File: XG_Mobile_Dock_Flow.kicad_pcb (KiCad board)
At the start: 4 copper layers, 220 x 65 mm, 111 parts, among them J1 5-1775443-8, J10 SWD, J11 UART, J12 I2C1, J13 39300240, J14 469911008, J17 8730, J2 20455-040E-76, J3 20455-040E-76, J4 3-2362375-4, J5 USB_C_Receptacle, Q16 AO3401A, Q17 2N7002W, SW1 SW_Push, U1 DS160PR410RNQR, U12 STM32F030C8Tx, U2 DS160PR410RNQR

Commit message: slight correction to 3.3v trace
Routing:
- net +3V3: track 237.6 -> 231.3 mm
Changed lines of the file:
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@@
-	)
-	(segment
-		(start 143.6 92.725)
-		(end 147.825 88.5)
-		(width 2.045295)
-		(layer "In1.Cu")
-		(net 2)
 	)
 	(segment
@@
 	)
 	(segment
-		(start 91.079446 78.920554)
-		(end 84.917496 72.758603)
-		(width 1.5)
+		(start 86.075 63.377496)
+		(end 85.382504 63.377496)
+		(width 2.045295)
 		(layer "In1.Cu")
 		(net 2)
@@
 	)
 	(segment
-		(start 147.825 83.040678)
-		(end 154.33666 76.529018)
-		(width 2.045295)
-		(layer "In1.Cu")
-		(net 2)
-	)
-	(segment
-		(start 104.883893 92.725)
-		(end 143.6 92.725)
-		(width 2.045295)
+		(start 84.917496 72.758604)
+		(end 84.917496 71.057504)
+		(width 1.5)
 		(layer "In1.Cu")
 		(net 2)
@@
 		(end 101.025 80.875)
 		(width 1.5)
+		(layer "In1.Cu")
+		(net 2)
+	)
+	(segment
+		(start 143.6 92.725)
+		(end 147.825 88.5)
+		(width 2.045295)
 		(layer "In1.Cu")
 		(net 2)
@@
 	)
 	(segment
-		(start 154.33666 76.529018)
-		(end 169.83666 76.529018)
-		(width 2.045295)
-		(layer "In1.Cu")
-		(net 2)
-	)
-	(segment
 		(start 98.425 74.025)
 		(end 95.975 74.025)
@@
 	)
 	(segment
+		(start 85.15 72.991107)
+		(end 104.883893 92.725)
+		(width 2.045295)
+		(layer "In1.Cu")
+		(net 2)
+	)
+	(segment
+		(start 105.275 79.425)
+		(end 105.275 80.875)
+		(width 1.5)
+		(layer "In1.Cu")
+		(net 2)
+	)
+	(segment
+		(start 107.925 80.875)
+		(end 105.275 80.875)
+		(width 0.8)
+		(layer "In1.Cu")
+		(net 2)
+	)
+	(segment
 		(start 147.825 88.5)
 		(end 147.825 83.040678)
@@
 	)
 	(segment
-		(start 84.917496 72.758603)
-		(end 104.312893 92.154)
-		(width 2.045295)
-		(layer "In1.Cu")
-		(net 2)
-	)
-	(segment
-		(start 105.275 79.425)
-		(end 105.275 80.875)
-		(width 1.5)
-		(layer "In1.Cu")
-		(net 2)
-	)
-	(segment
-		(start 107.925 80.875)
-		(end 105.275 80.875)
-		(width 0.8)
+		(start 147.825 83.040678)
+		(end 154.33666 76.529018)
+		(width 2.045295)
 		(layer "In1.Cu")
 		(net 2)
@@
 		(end 97.029446 84.870554)
 		(width 1.5)
+		(layer "In1.Cu")
+		(net 2)
+	)
+	(segment
+		(start 154.33666 76.529018)
+		(end 169.83666 76.529018)
+		(width 2.045295)
+		(layer "In1.Cu")
+		(net 2)
+	)
+	(segment
+		(start 104.883893 92.725)
+		(end 143.6 92.725)
+		(width 2.045295)
 		(layer "In1.Cu")
 		(net 2)
@@
 	)
 	(segment
-		(start 84.917496 63.377496)
-		(end 84.917496 72.758603)
-		(width 2.045295)
-		(layer "In1.Cu")
-		(net 2)
-	)
-	(segment
-		(start 104.312893 92.154)
-		(end 104.883893 92.725)
+		(start 85.15 63.61)
+		(end 85.15 72.526099)
+		(width 2.045295)
+		(layer "In1.Cu")
+		(net 2)
+	)
+	(segment
+		(start 85.15 70.825)
+		(end 85.15 72.991107)
+		(width 2.045295)
+		(layer "In1.Cu")
+		(net 2)
+	)
+	(segment
+		(start 85.382504 63.377496)
+		(end 85.15 63.61)
 		(width 2.045295)
 		(layer "In1.Cu")
@@
 	)
 	(segment
-		(start 84.917496 63.377496)
-		(end 86.917496 63.377496)
-		(width 1.5)
-		(layer "In1.Cu")
+		(start 84.917496 71.057504)
+		(end 85.15 70.825)
+		(width 1.5)
+		(layer "In1.Cu")

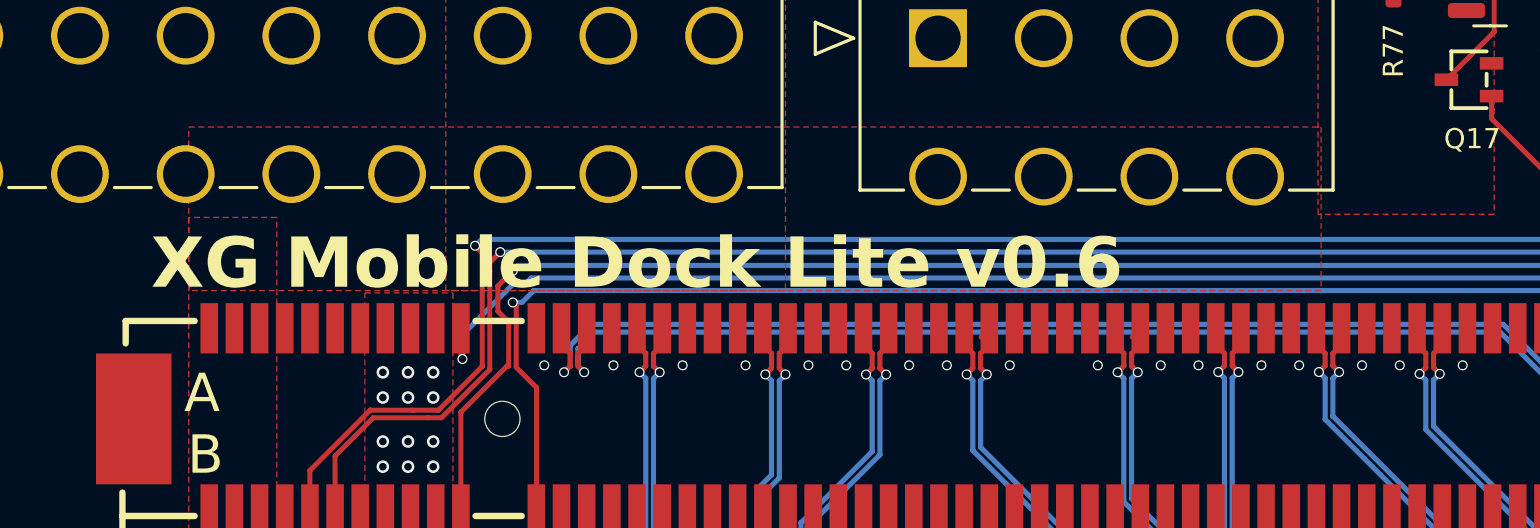
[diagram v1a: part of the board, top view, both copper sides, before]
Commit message: added proper text on board
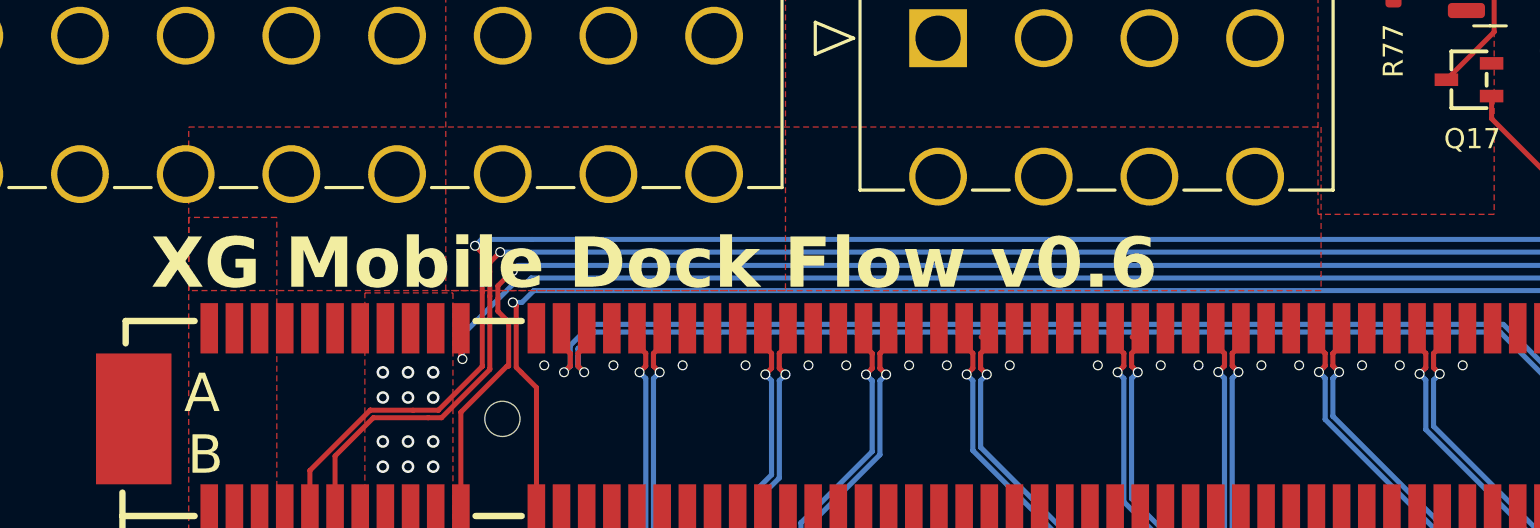
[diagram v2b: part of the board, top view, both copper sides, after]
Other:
- board text added: "XG Mobile Dock Flow v0.6"
- board text removed: "XG Mobile Dock Lite v0.6"
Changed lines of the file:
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@@
 		)
 	)
-	(gr_text "XG Mobile Dock Lite v0.6"
+	(gr_text "XG Mobile Dock Flow v0.6"
 		(at 75.621496 55.121496 0)
 		(layer "F.SilkS")

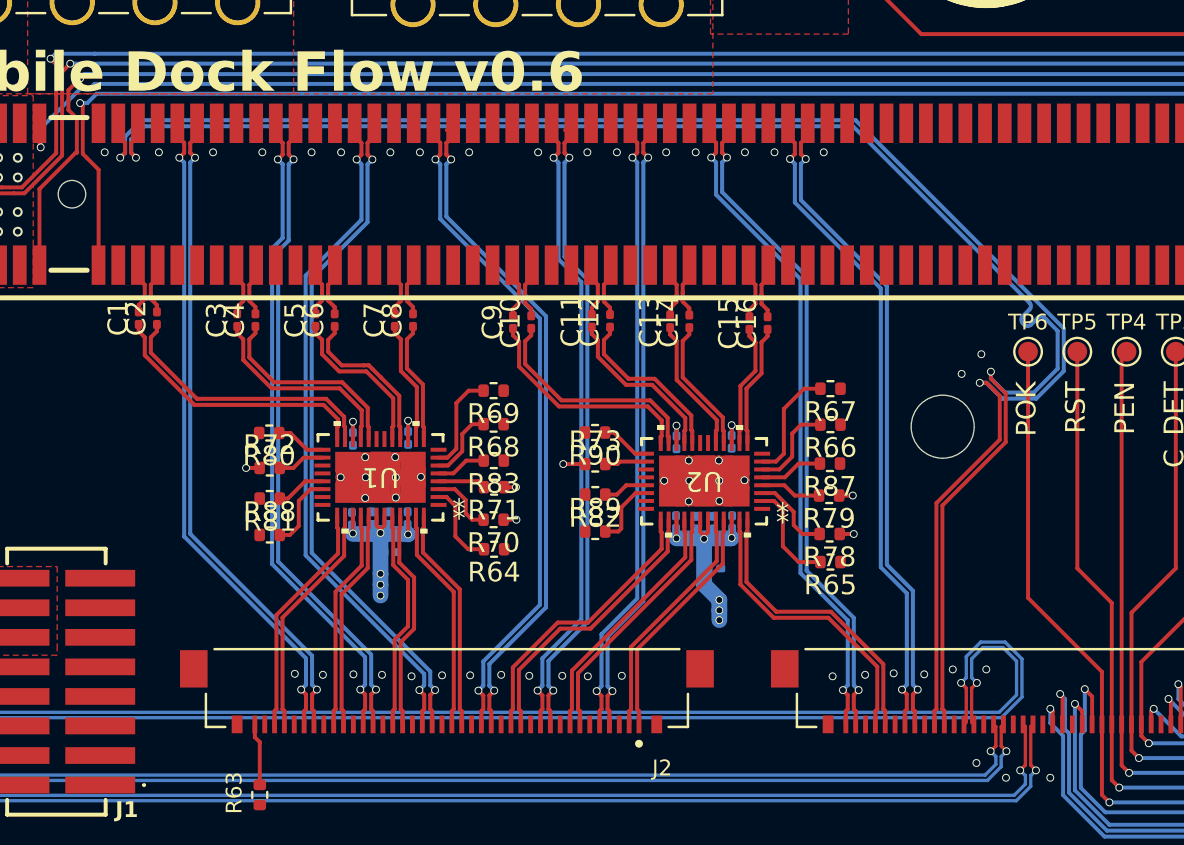
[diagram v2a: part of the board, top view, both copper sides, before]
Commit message: better routing of the pcie clock trace
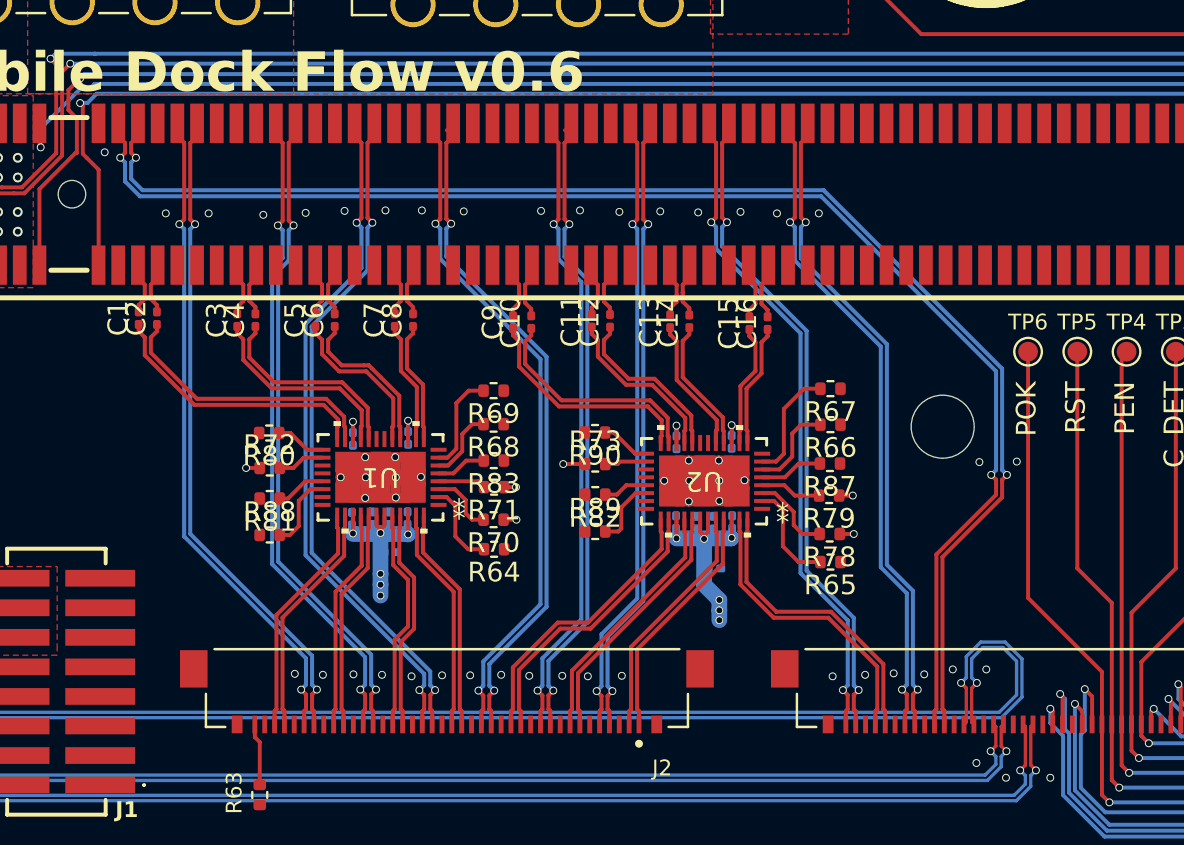
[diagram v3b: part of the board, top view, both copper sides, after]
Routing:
- net /CLKP: track 82.4 -> 71.0 mm
- net /CLKN: track 82.3 -> 71.0 mm

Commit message: final changes, still need to recheck
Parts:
- removed J16: ~, Connector_JST:JST_PH_S2B-PH-K_1x02_P2.00mm_Horizontal
- removed R74: 47k, Resistor_SMD:R_0402_1005Metric
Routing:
- net GND: vias 66 -> 76

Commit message: more preparations for building the board
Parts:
- C1, C10, C11, C12, C13, C14, C15, C16, C2, C3, C4, C5, C6, C7, C8, C9: value 0.22μF -> 220nF
- C17, C18, C19, C20, C22, C23, C24, C25: value 0.1μF -> 100nF
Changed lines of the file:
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@@
 			(outputformat 1)
 			(mirror no)
-			(drillshape 1)
+			(drillshape 0)
 			(scaleselection 1)
-			(outputdirectory "")
+			(outputdirectory "../XG_Mobile_Station_Release/")
 		)
 	)
@@
 			)
 		)
-		(property "Value" "0.22μF"
+		(property "Value" "220nF"
 			(at 0 1.05 90)
 			(layer "F.Fab")
@@
 			)
 		)
-		(property "Value" "0.22μF"
+		(property "Value" "220nF"
 			(at 0 1.05 90)
 			(layer "F.Fab")
@@
 		(sheetname "/")
 		(sheetfile "XG_Mobile_Dock_Flow.kicad_sch")
-		(attr through_hole exclude_from_pos_files)
+		(attr through_hole)
 		(fp_line
 			(start 4.877981 0.635)
@@
 			)
 		)
-		(property "Value" "0.22μF"
+		(property "Value" "220nF"
 			(at 0 1.05 90)
 			(layer "F.Fab")
@@
 			)
 		)
-		(property "Value" "0.22μF"
+		(property "Value" "220nF"
 			(at 0 1.05 90)
 			(layer "F.Fab")
@@
 			)
 		)
-		(property "Value" "0.22μF"
+		(property "Value" "220nF"
 			(at 0 1.05 90)
 			(layer "F.Fab")
@@
 			)
 		)
-		(property "Value" "0.22μF"
+		(property "Value" "220nF"
 			(at 0 1.05 90)
 			(layer "F.Fab")
@@
 			)
 		)
-		(property "Value" "0.22μF"
+		(property "Value" "220nF"
 			(at 0 1.05 90)
 			(layer "F.Fab")
@@
 			)
 		)
-		(property "Value" "0.22μF"
+		(property "Value" "220nF"
 			(at 0 1.05 90)
 			(layer "F.Fab")
@@
 			)
 		)
-		(property "Value" "0.22μF"
+		(property "Value" "220nF"
 			(at 0 1.05 90)
 			(layer "F.Fab")
@@
 			)
 		)
-		(property "Value" "0.22μF"
+		(property "Value" "220nF"
 			(at 0 1.05 90)
 			(layer "F.Fab")
@@
 			)
 		)
-		(property "Value" "0.22μF"
+		(property "Value" "220nF"
 			(at 0 1.05 90)
 			(layer "F.Fab")
@@
 			)
 		)
-		(property "Value" "0.22μF"
+		(property "Value" "220nF"
 			(at 0 1.05 90)
 			(layer "F.Fab")
@@
 			)
 		)
-		(property "Value" "0.22μF"
+		(property "Value" "220nF"
 			(at 0 1.05 90)
 			(layer "F.Fab")
@@
 			)
 		)
-		(property "Value" "0.22μF"
+		(property "Value" "220nF"
 			(at 0 1.05 90)
 			(layer "F.Fab")
@@
 		)
 		(fp_text user "*"
-			(at -3.9878 -1.6 180)
-			(unlocked yes)
+			(at -3.9878 -1.6 0)
 			(layer "F.SilkS")
 			(effects
@@
 		)
 		(fp_text user "*"
-			(at -3.9878 -1.6 0)
+			(at -3.9878 -1.6 180)
+			(unlocked yes)
 			(layer "F.SilkS")
 			(effects
@@
 		)
 		(fp_text user "*"
-			(at -2.54 -1.6 180)
-			(unlocked yes)
+			(at -2.54 -1.6 0)
 			(layer "F.Fab")
 			(effects
@@
 		)
 		(fp_text user "*"
-			(at -2.54 -1.6 0)
+			(at -2.54 -1.6 180)
+			(unlocked yes)
 			(layer "F.Fab")
 			(effects
@@
 			)
 		)
-		(property "Value" "0.22μF"
+		(property "Value" "220nF"
 			(at 0 1.05 90)
 			(layer "F.Fab")
@@
 			)
 		)
-		(property "Value" "0.22μF"
+		(property "Value" "220nF"
 			(at 0 1.05 90)
 			(layer "F.Fab")
@@
 			)
 		)
-		(property "Value" "0.1μF"
+		(property "Value" "100nF"
 			(at 0 -1.05 90)
 			(layer "B.Fab")
@@
 			)
 		)
-		(property "Value" "0.1μF"
+		(property "Value" "100nF"
 			(at 0 -1.05 90)
 			(layer "B.Fab")
@@
 			)
 		)
-		(property "Value" "0.1μF"
+		(property "Value" "100nF"
 			(at 0 -1.05 90)
 			(layer "B.Fab")
@@
 			)
 		)
-		(property "Value" "0.1μF"
+		(property "Value" "100nF"
 			(at 0 -1.05 90)
 			(layer "B.Fab")
@@
 			)
 		)
-		(property "Value" "0.1μF"
+		(property "Value" "100nF"
 			(at 0 -1.05 90)
 			(layer "B.Fab")
@@
 			)
 		)
-		(property "Value" "0.1μF"
+		(property "Value" "100nF"
 			(at 0 -1.05 90)
 			(layer "B.Fab")
@@
 			)
 		)
-		(property "Value" "0.1μF"
+		(property "Value" "100nF"
 			(at 0 -1.05 90)
 			(layer "B.Fab")
@@
 			)
 		)
-		(property "Value" "0.1μF"
+		(property "Value" "100nF"
 			(at 0 -1.05 90)
 			(layer "B.Fab")
